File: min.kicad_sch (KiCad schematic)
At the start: 0 parts

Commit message: adding the time seting buttons
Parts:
- added SW1: SW_MEC_5G, Button_Switch_SMD:SW_MEC_5GSH9, symbol Switch:SW_MEC_5G
- added U4: 4081, symbol 4xxx:4081
- added U7, U9: 4510, symbol 4xxx:4510
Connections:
- new net: U4.10, U7.9 (RST), U9.15 (CLK)
- new net: SW1.1 (A), SW1.2 (A)
- new net: SW1.3 (B), SW1.4 (B)
- new net +5V: U7.10 (U/D), U7.16 (VDD), U9.10 (U/D), U9.16 (VDD)
- new net CLK: U7.15 (CLK)
- new net GND: U7.1 (PE), U7.12 (A2), U7.13 (A3), U7.3 (A4), U7.4 (A1), U7.5 (CI), U7.8 (VSS), U9.1 (PE), U9.12 (A2), U9.13 (A3), U9.3 (A4), U9.4 (A1), U9.5 (CI), U9.8 (VSS)
- new net min-o_1: U7.6 (Q1)
- new net min-o_2: U4.8, U7.11 (Q2)
- new net min-o_3: U7.14 (Q3)
- new net min-o_4: U4.9, U7.2 (Q4)
- new net min-t_1: U9.6 (Q1)
- new net min-t_2: U4.12, U9.11 (Q2)
- new net min-t_3: U4.13, U9.14 (Q3)
- new net min-t_4: U9.2 (Q4)
- new net min_clk: U4.11, U9.9 (RST)

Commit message: finishing the min circuit
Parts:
- added C3, C4: 100nF, symbol Device:C
- added R3, R5: 10k, symbol Device:R
- added R4, R6: 100k, symbol Device:R
- added SW2, SW3: SW_MEC_5G, Button_Switch_SMD:SW_MEC_5GSH9, symbol Switch:SW_MEC_5G
- added U8: 4071, symbol 4xxx:4071
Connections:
- net +5V: now also SW1.1 (A), SW1.2 (A), SW2.1 (A), SW2.2 (A), U8.14 (VDD)
- net CLK: now also U8.13; no longer U7.15 (CLK)
- net GND: now also C3.1, C4.1, R4.2, R6.2, U8.7 (VSS)
- net at U4.10, U7.9 (RST): now also U8.2; no longer U9.15 (CLK)
- net at SW1.3 (B), SW1.4 (B): now also R3.1, R4.1
- new net: U7.15 (CLK), U8.11
- new net: R5.1, R6.1, SW2.3 (B), SW2.4 (B)
- new net: C4.2, R5.2, U8.1
- new net: U8.3, U9.15 (CLK)
- new net: SW3.1 (A), SW3.2 (A)
- new net: SW3.3 (B), SW3.4 (B)
- new net: C3.2, R3.2, U8.12
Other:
- moved on the sheet: SW1

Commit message: finishing the min circuit nad conect it to its place
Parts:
- removed SW3: SW_MEC_5G, Button_Switch_SMD:SW_MEC_5GSH9, symbol Switch:SW_MEC_5G
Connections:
- net min_clk renamed h_clk
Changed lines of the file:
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@@
 		)
 	)
-	(hierarchical_label "min_clk"
+	(hierarchical_label "h_clk"
 		(shape output)
 		(at 228.6 71.12 0)
@@
 					(unit 1)
 				)
-			)
-		)
-	)
-	(symbol
-		(lib_id "Switch:SW_MEC_5G")
-		(at 196.85 33.02 0)
-		(unit 1)
-		(body_style 1)
-		(exclude_from_sim no)
-		(in_bom yes)
-		(on_board yes)
-		(in_pos_files yes)
-		(dnp no)
-		(fields_autoplaced yes)
-		(property "Reference" "SW3"
-			(at 196.85 25.4 0)
-			(show_name no)
-			(do_not_autoplace no)
-			(effects
-				(font
-					(size 1.27 1.27)
-				)
-			)
-		)
-		(property "Value" "SW_MEC_5G"
-			(at 196.85 27.94 0)
-			(show_name no)
-			(do_not_autoplace no)
-			(effects
-				(font
-					(size 1.27 1.27)
-				)
-			)
-		)
-		(property "Footprint" "Button_Switch_SMD:SW_MEC_5GSH9"
-			(at 196.85 27.94 0)
-			(hide yes)
-			(show_name no)
-			(do_not_autoplace no)
-			(effects
-				(font
-					(size 1.27 1.27)
-				)
-			)
-		)
-		(property "Datasheet" "https://www.apem.com/medias/download/MEC_switches_serie_MULTIMEC5G.pdf"
-			(at 196.85 27.94 0)
-			(hide yes)
-			(show_name no)
-			(do_not_autoplace no)
-			(effects
-				(font
-					(size 1.27 1.27)
-				)
-			)
-		)
-		(property "Description" "MEC 5G single pole normally-open tactile switch"
-			(at 196.85 33.02 0)
-			(hide yes)
-			(show_name no)
-			(do_not_autoplace no)
-			(effects
-				(font
-					(size 1.27 1.27)
-				)
-			)
-		)
-		(pin "1"
-		)
-		(pin "3"
-		)
-		(pin "4"
-		)
-		(pin "2"
-		)
-		(instances
-			(project "BinaryClock"
-				(path "/b8db7867-2c41-4996-89b7-85623a375f4b/d72dbc43-5f9c-4389-b46b-bcc9f20f0691/8f29d748-f0e9-4594-b3bf-d81643fe275d"
-					(reference "SW3")
-					(unit 1)
-				)

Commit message: creating the file and copiing the template
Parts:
- removed unit 2 of U8
- removed unit 3 of U8
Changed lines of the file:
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@@
-	)
-	(symbol
-		(lib_id "4xxx:4071")
-		(at 107.95 139.7 0)
-		(unit 2)
-		(body_style 1)
-		(exclude_from_sim no)
-		(in_bom yes)
-		(on_board yes)
-		(in_pos_files yes)
-		(dnp no)
-		(fields_autoplaced yes)
-		(property "Reference" "U8"
-			(at 107.95 130.81 0)
-			(show_name no)
-			(do_not_autoplace no)
-			(effects
-				(font
-					(size 1.27 1.27)
-				)
-			)
-		)
-		(property "Value" "4071"
-			(at 107.95 133.35 0)
-			(show_name no)
-			(do_not_autoplace no)
-			(effects
-				(font
-					(size 1.27 1.27)
-				)
-			)
-		)
-		(property "Footprint" ""
-			(at 107.95 139.7 0)
-			(hide yes)
-			(show_name no)
-			(do_not_autoplace no)
-			(effects
-				(font
-					(size 1.27 1.27)
-				)
-			)
-		)
-		(property "Datasheet" "http://www.intersil.com/content/dam/Intersil/documents/cd40/cd4071bms-72bms-75bms.pdf"
-			(at 107.95 139.7 0)
-			(hide yes)
-			(show_name no)
-			(do_not_autoplace no)
-			(effects
-				(font
-					(size 1.27 1.27)
-				)
-			)
-		)
-		(property "Description" "Quad Or 2 inputs"
-			(at 107.95 139.7 0)
-			(hide yes)
-			(show_name no)
-			(do_not_autoplace no)
-			(effects
-				(font
-					(size 1.27 1.27)
-				)
-			)
-		)
-		(pin "9"
-		)
-		(pin "12"
-		)
-		(pin "5"
-		)
-		(pin "7"
-		)
-		(pin "8"
-		)
-		(pin "3"
-		)
-		(pin "2"
-		)
-		(pin "1"
-		)
-		(pin "4"
-		)
-		(pin "6"
-		)
-		(pin "10"
-		)
-		(pin "11"
-		)
-		(pin "13"
-		)
-		(pin "14"
-		)
-		(instances
-			(project "BinaryClock"
-				(path "/b8db7867-2c41-4996-89b7-85623a375f4b/d72dbc43-5f9c-4389-b46b-bcc9f20f0691/8f29d748-f0e9-4594-b3bf-d81643fe275d"
-					(reference "U8")
-					(unit 2)
-				)
-			)
-		)
 	)
 	(symbol
@@
 				)
 			)
-		)
-	)
-	(symbol
-		(lib_id "4xxx:4071")
-		(at 107.95 148.59 0)
-		(unit 3)
-		(body_style 1)
-		(exclude_from_sim no)
-		(in_bom yes)
-		(on_board yes)
-		(in_pos_files yes)
-		(dnp no)
-		(fields_autoplaced yes)
-		(property "Reference" "U8"
-			(at 107.95 139.7 0)
-			(show_name no)
-			(do_not_autoplace no)
-			(effects
-				(font
-					(size 1.27 1.27)
-				)
-			)
-		)
-		(property "Value" "4071"
-			(at 107.95 142.24 0)
-			(show_name no)
-			(do_not_autoplace no)
-			(effects
-				(font
-					(size 1.27 1.27)
-				)
-			)
-		)
-		(property "Footprint" ""
-			(at 107.95 148.59 0)
-			(hide yes)
-			(show_name no)
-			(do_not_autoplace no)
-			(effects
-				(font
-					(size 1.27 1.27)
-				)
-			)
-		)
-		(property "Datasheet" "http://www.intersil.com/content/dam/Intersil/documents/cd40/cd4071bms-72bms-75bms.pdf"
-			(at 107.95 148.59 0)
-			(hide yes)
-			(show_name no)
-			(do_not_autoplace no)
-			(effects
-				(font
-					(size 1.27 1.27)
-				)
-			)
-		)
-		(property "Description" "Quad Or 2 inputs"
-			(at 107.95 148.59 0)
-			(hide yes)
-			(show_name no)
-			(do_not_autoplace no)
-			(effects
-				(font
-					(size 1.27 1.27)
-				)
-			)
-		)
-		(pin "9"
-		)
-		(pin "12"
-		)
-		(pin "5"
-		)
-		(pin "7"
-		)
-		(pin "8"
-		)
-		(pin "3"
-		)
-		(pin "2"
-		)
-		(pin "1"
-		)
-		(pin "4"
-		)
-		(pin "6"
-		)
-		(pin "10"
-		)
-		(pin "11"
-		)
-		(pin "13"
-		)
-		(pin "14"
-		)
-		(instances
-			(project "BinaryClock"
-				(path "/b8db7867-2c41-4996-89b7-85623a375f4b/d72dbc43-5f9c-4389-b46b-bcc9f20f0691/8f29d748-f0e9-4594-b3bf-d81643fe275d"
-					(reference "U8")
-					(unit 3)
-				)
-			)

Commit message: Making the circuit for the hour counter
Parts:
- renumbered U4 to U3, U8 to U6, U9 to U8

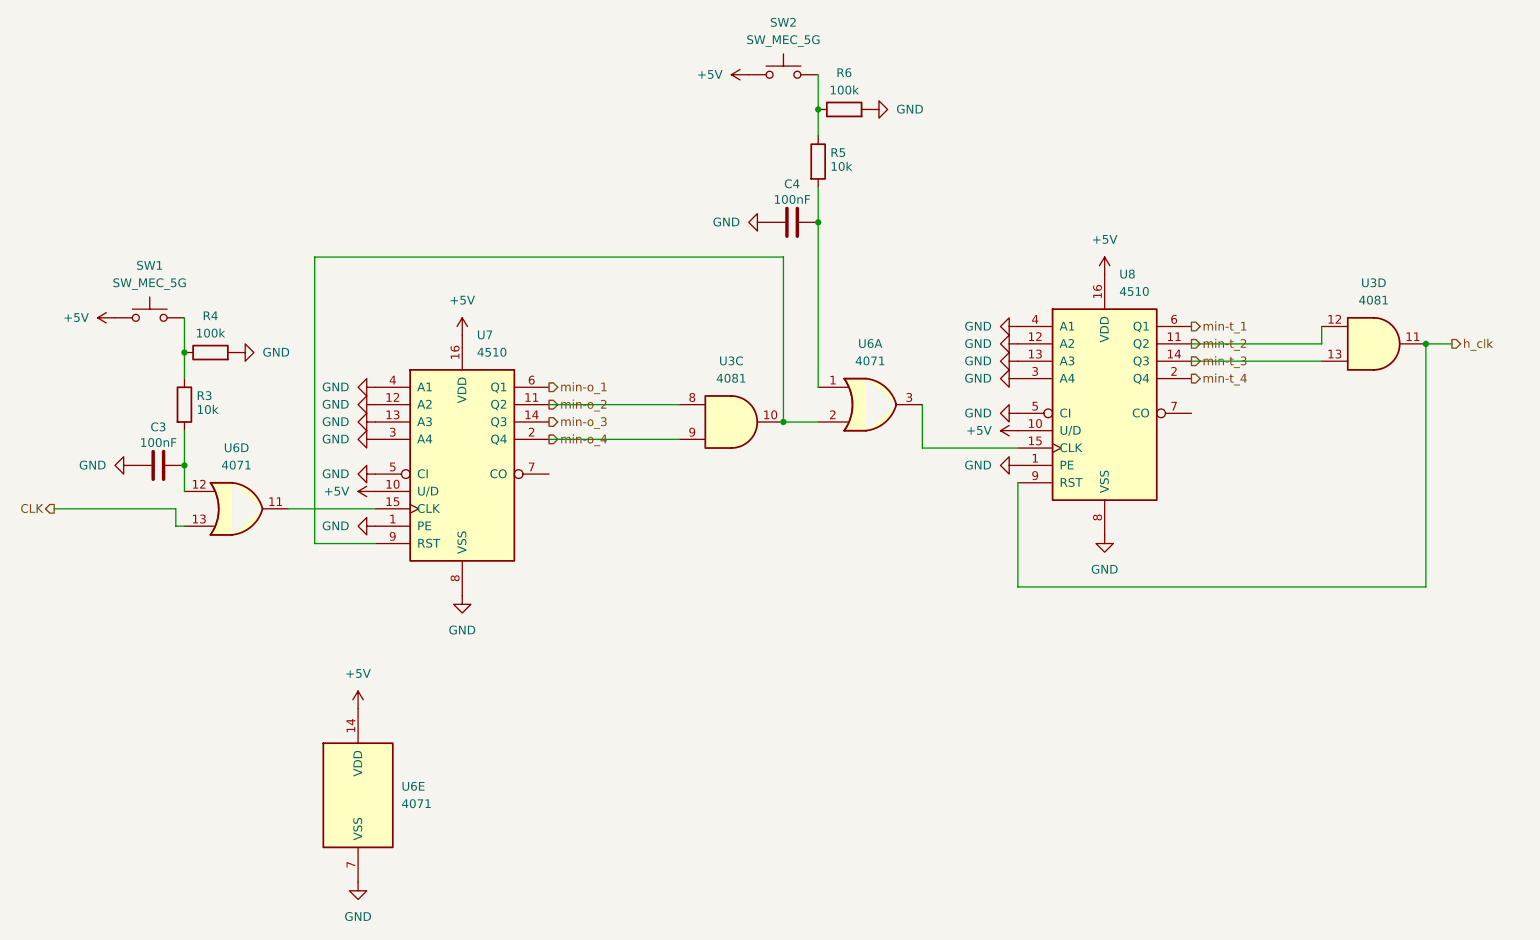
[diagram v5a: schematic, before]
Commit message: Making the 24 rst for ewery counter and adding Capacitors
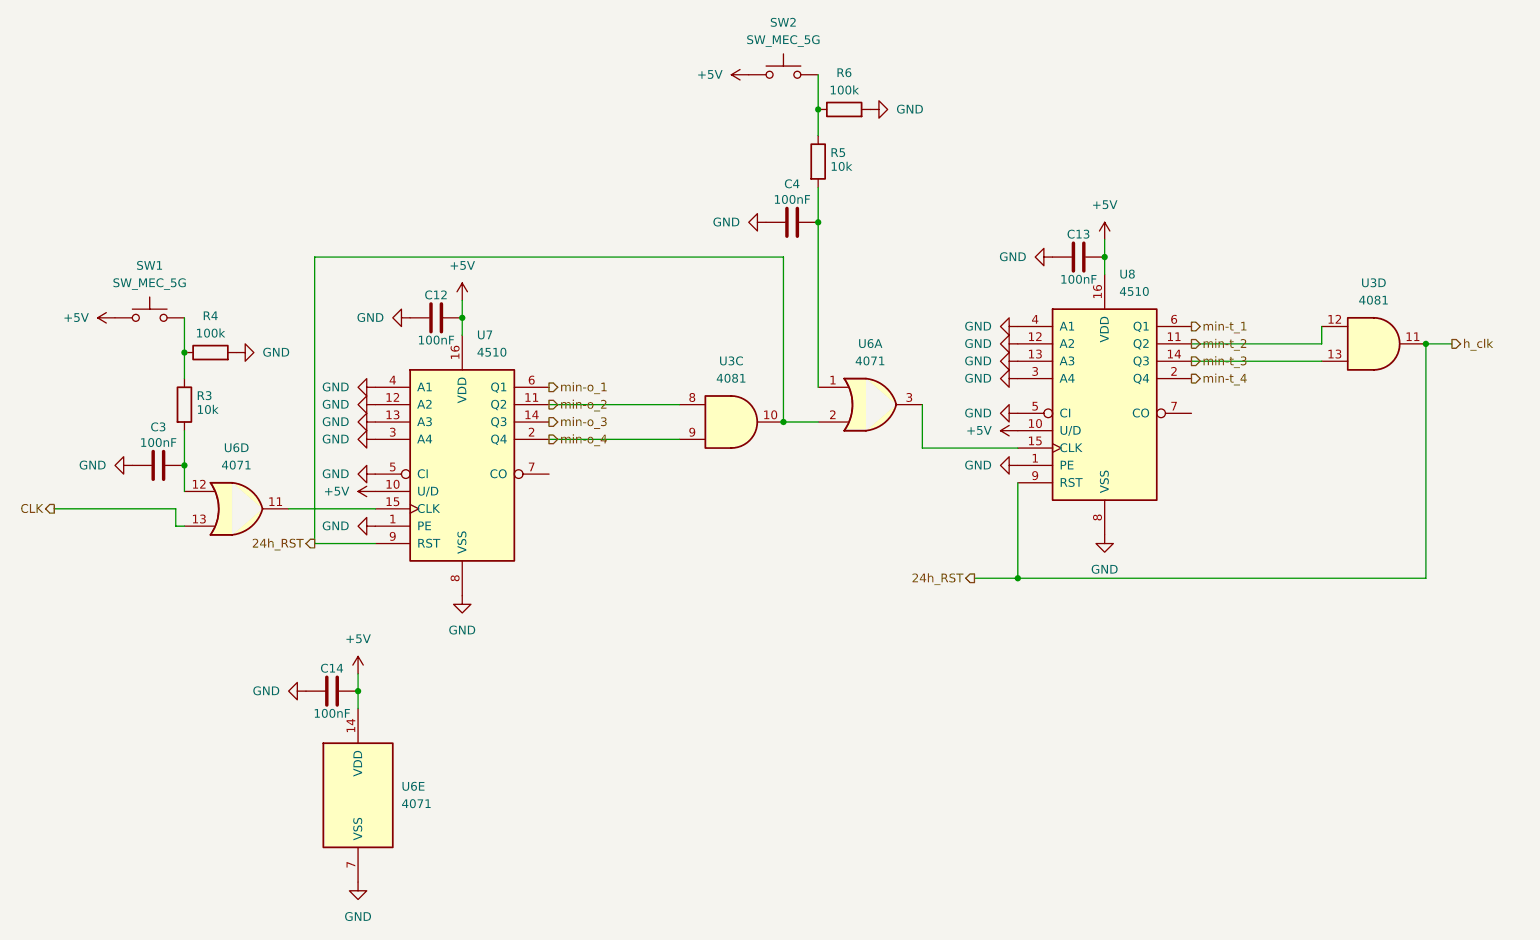
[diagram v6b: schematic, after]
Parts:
- added C12, C13, C14: 100nF, symbol Device:C
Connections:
- net h_clk is gone; now on net 24h_RST: U3.11, U8.9 (RST)
- net +5V: now also C12.2, C13.2, C14.2
- net GND: now also C12.1, C13.1, C14.1
- net 24h_RST: now reaches U3.10, U6.2, U7.9 (RST)

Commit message: Cleaning the shematic
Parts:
- renumbered C12 to C10, C4 to C11, C13 to C12, C3 to C8, C14 to C9

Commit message: finishing the footprint asigment
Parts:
- C10, C11, C12, C8, C9: footprint (none) -> Resistor_SMD:R_0603_1608Metric; LCSC Part (none) -> C1591
- R3, R5: footprint (none) -> Resistor_SMD:R_0603_1608Metric; LCSC Part (none) -> C98220
- R4, R6: footprint (none) -> Resistor_SMD:R_0603_1608Metric; LCSC Part (none) -> C14675
- SW1, SW2: footprint Button_Switch_SMD:SW_MEC_5GSH9 -> Button_Switch_THT:SW_PUSH_6mm_H5mm; LCSC Part (none) -> C42416244
- U3: footprint (none) -> Package_SO:SOIC-14_3.9x8.7mm_P1.27mm; LCSC Part (none) -> C40551
- U6: footprint (none) -> Package_SO:SOIC-14_3.9x8.7mm_P1.27mm; LCSC Part (none) -> C97039
- U7, U8: footprint (none) -> Package_SO:TSSOP-16_4.4x5mm_P0.65mm; LCSC Part (none) -> C2862976
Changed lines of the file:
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@@
 			)
 		)
-		(property "Footprint" ""
+		(property "Footprint" "Package_SO:SOIC-14_3.9x8.7mm_P1.27mm"
 			(at 217.17 71.12 0)
 			(hide yes)
@@
 			)
 		)
+		(property "LCSC Part" "C40551"
+			(at 217.17 71.12 0)
+			(hide yes)
+			(show_name no)
+			(do_not_autoplace no)
+			(effects
+				(font
+					(size 1.27 1.27)
+				)
+			)
+		)
 		(pin "4"
 		)
@@
 			)
 		)
-		(property "Footprint" ""
+		(property "Footprint" "Resistor_SMD:R_0603_1608Metric"
 			(at 46.99 74.168 90)
 			(hide yes)
@@
 			)
 		)
+		(property "LCSC Part" "C14675"
+			(at 46.99 72.39 90)
+			(hide yes)
+			(show_name no)
+			(do_not_autoplace no)
+			(effects
+				(font
+					(size 1.27 1.27)
+				)
+			)
+		)
 		(pin "2"
 		)
@@
 			)
 		)
-		(property "Footprint" ""
+		(property "Footprint" "Package_SO:TSSOP-16_4.4x5mm_P0.65mm"
 			(at 83.82 87.63 0)
 			(hide yes)
@@
 			)
 		)
+		(property "LCSC Part" "C2862976"
+			(at 83.82 87.63 0)
+			(hide yes)
+			(show_name no)
+			(do_not_autoplace no)
+			(effects
+				(font
+					(size 1.27 1.27)
+				)
+			)
+		)
 		(pin "12"
 		)
@@
 			)
 		)
-		(property "Footprint" ""
+		(property "Footprint" "Resistor_SMD:R_0603_1608Metric"
 			(at 139.7 38.608 90)
 			(hide yes)
@@
 			)
 		)
+		(property "LCSC Part" "C14675"
+			(at 139.7 36.83 90)
+			(hide yes)
+			(show_name no)
+			(do_not_autoplace no)
+			(effects
+				(font
+					(size 1.27 1.27)
+				)
+			)
+		)
 		(pin "2"
 		)
@@
 			)
 		)
-		(property "Footprint" ""
+		(property "Footprint" "Package_SO:SOIC-14_3.9x8.7mm_P1.27mm"
 			(at 68.58 137.16 0)
 			(hide yes)
@@
 			)
 		)
+		(property "LCSC Part" "C97039"
+			(at 68.58 137.16 0)
+			(hide yes)
+			(show_name no)
+			(do_not_autoplace no)
+			(effects
+				(font
+					(size 1.27 1.27)
+				)
+			)
+		)
 		(pin "9"
 		)
@@
 			)
 		)
-		(property "Footprint" ""
+		(property "Footprint" "Package_SO:SOIC-14_3.9x8.7mm_P1.27mm"
 			(at 123.19 82.55 0)
 			(hide yes)
@@
 			)
 		)
+		(property "LCSC Part" "C40551"
+			(at 123.19 82.55 0)
+			(hide yes)
+			(show_name no)
+			(do_not_autoplace no)
+			(effects
+				(font
+					(size 1.27 1.27)
+				)
+			)
+		)
 		(pin "4"
 		)
@@
 			)
 		)
-		(property "Footprint" ""
+		(property "Footprint" "Package_SO:SOIC-14_3.9x8.7mm_P1.27mm"
 			(at 143.51 80.01 0)
 			(hide yes)
@@
 			)
 		)
+		(property "LCSC Part" "C97039"
+			(at 143.51 80.01 0)
+			(hide yes)
+			(show_name no)
+			(do_not_autoplace no)
+			(effects
+				(font
+					(size 1.27 1.27)
+				)
+			)
+		)
 		(pin "9"
 		)
@@
 			)
 		)
-		(property "Footprint" ""
+		(property "Footprint" "Resistor_SMD:R_0603_1608Metric"
 			(at 134.112 44.45 90)
 			(hide yes)
@@
 			)
 		)
+		(property "LCSC Part" "C98220"
+			(at 135.89 44.45 0)
+			(hide yes)
+			(show_name no)
+			(do_not_autoplace no)
+			(effects
+				(font
+					(size 1.27 1.27)
+				)
+			)
+		)
 		(pin "2"
 		)
@@
 			)
 		)
-		(property "Footprint" ""
+		(property "Footprint" "Resistor_SMD:R_0603_1608Metric"
 			(at 177.8 57.4548 0)
 			(hide yes)
@@
 			)
 		)
+		(property "LCSC Part" "C1591"
+			(at 173.99 58.42 90)
+			(hide yes)
+			(show_name no)
+			(do_not_autoplace no)
+			(effects
+				(font
+					(size 1.27 1.27)
+				)
+			)
+		)
 		(pin "1"
 		)
@@
 			)
 		)
-		(property "Footprint" ""
+		(property "Footprint" "Resistor_SMD:R_0603_1608Metric"
 			(at 68.58 120.9548 0)
 			(hide yes)
@@
 			)
 		)
+		(property "LCSC Part" "C1591"
+			(at 64.77 121.92 90)
+			(hide yes)
+			(show_name no)
+			(do_not_autoplace no)
+			(effects
+				(font
+					(size 1.27 1.27)
+				)
+			)
+		)
 		(pin "1"
 		)
@@
 			)
 		)
-		(property "Footprint" ""
+		(property "Footprint" "Resistor_SMD:R_0603_1608Metric"
 			(at 41.402 80.01 90)
 			(hide yes)
@@
 			)
 		)
+		(property "LCSC Part" "C98220"
+			(at 43.18 80.01 0)
+			(hide yes)
+			(show_name no)
+			(do_not_autoplace no)
+			(effects
+				(font
+					(size 1.27 1.27)
+				)
+			)
+		)
 		(pin "2"
 		)
@@
 			)
 		)
-		(property "Footprint" "Button_Switch_SMD:SW_MEC_5GSH9"
+		(property "Footprint" "Button_Switch_THT:SW_PUSH_6mm_H5mm"
 			(at 130.81 26.67 0)
 			(hide yes)
@@
 			)
 		)
+		(property "LCSC Part" "C42416244"
+			(at 130.81 31.75 0)
+			(hide yes)
+			(show_name no)
+			(do_not_autoplace no)
+			(effects
+				(font
+					(size 1.27 1.27)
+				)
+			)
+		)
 		(pin "1"
 		)
@@
 			)
 		)
-		(property "Footprint" "Button_Switch_SMD:SW_MEC_5GSH9"
+		(property "Footprint" "Button_Switch_THT:SW_PUSH_6mm_H5mm"
 			(at 38.1 62.23 0)
 			(hide yes)
@@
 			)
 		)
+		(property "LCSC Part" "C42416244"
+			(at 38.1 67.31 0)
+			(hide yes)
+			(show_name no)
+			(do_not_autoplace no)
+			(effects
+				(font
+					(size 1.27 1.27)
+				)
+			)
+		)
 		(pin "1"
 		)
@@
 			)
 		)
-		(property "Footprint" ""
+		(property "Footprint" "Package_SO:SOIC-14_3.9x8.7mm_P1.27mm"
 			(at 50.8 95.25 0)
 			(hide yes)
@@
 			)
 		)
+		(property "LCSC Part" "C97039"
+			(at 50.8 95.25 0)
+			(hide yes)
+			(show_name no)
+			(do_not_autoplace no)
+			(effects
+				(font
+					(size 1.27 1.27)
+				)
+			)
+		)
 		(pin "9"
 		)
@@
 			)
 		)
-		(property "Footprint" ""
+		(property "Footprint" "Resistor_SMD:R_0603_1608Metric"
 			(at 43.18 87.9348 0)
 			(hide yes)
@@
 			)
 		)
+		(property "LCSC Part" "C1591"
+			(at 39.37 88.9 90)
+			(hide yes)
+			(show_name no)
+			(do_not_autoplace no)
+			(effects
+				(font
+					(size 1.27 1.27)
+				)
+			)
+		)
 		(pin "1"
 		)
@@
 			)
 		)
-		(property "Footprint" ""
+		(property "Footprint" "Package_SO:TSSOP-16_4.4x5mm_P0.65mm"
 			(at 177.8 78.74 0)
 			(hide yes)
@@
 			)
 		)
+		(property "LCSC Part" "C2862976"
+			(at 177.8 78.74 0)
+			(hide yes)
+			(show_name no)
+			(do_not_autoplace no)
+			(effects
+				(font
+					(size 1.27 1.27)
+				)
+			)
+		)
 		(pin "12"
 		)
@@
 			)
 		)
-		(property "Footprint" ""
+		(property "Footprint" "Resistor_SMD:R_0603_1608Metric"
 			(at 135.89 52.3748 0)
 			(hide yes)
@@
 			)
 		)
+		(property "LCSC Part" "C1591"
+			(at 132.08 53.34 90)
+			(hide yes)
+			(show_name no)
+			(do_not_autoplace no)
+			(effects
+				(font
+					(size 1.27 1.27)
+				)
+			)
+		)
 		(pin "1"
 		)
@@
 			)
 		)
-		(property "Footprint" ""
+		(property "Footprint" "Resistor_SMD:R_0603_1608Metric"
 			(at 83.82 66.3448 0)
 			(hide yes)
@@
 			(hide yes)
 			(show_name no)
+			(do_not_autoplace no)
+			(effects
+				(font
+					(size 1.27 1.27)
+				)
+			)
+		)
+		(property "LCSC Part" "C1591"
+			(at 80.01 67.31 90)
+			(hide yes)
+			(show_name no)
